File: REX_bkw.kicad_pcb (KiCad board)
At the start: 2 copper layers, 16 x 38 mm, 11 parts, among them J1 Molex_DIP28_edge_contacts, J2 JTAG, J3 PRG, U1 XCR3064XL-10VQ44, U2 29F800, U3 LP2980

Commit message: names
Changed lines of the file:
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@@
   (layers
     (0 Top signal)
-    (31 Bottom signal hide)
+    (31 Bottom signal)
     (32 B.Adhes user hide)
     (33 F.Adhes user hide)
@@
     (descr "Castellated edge contacts to fit Molex 8878 Socket")
     (solder_mask_margin -0.28)
+    (attr virtual)
     (fp_text reference J1 (at -0.9906 -0.9906 -90) (layer Dwgs.User) hide
       (effects (font (size 1.2065 1.2065) (thickness 0.127)) (justify left bottom))
@@
     (descr "Castellated edge contacts to fit Molex 8878 Socket")
     (solder_mask_margin -0.28)
+    (attr virtual)
     (fp_text reference carrier? (at -1.5 0 -90) (layer Dwgs.User) hide
       (effects (font (size 1.2065 1.2065) (thickness 0.127)) (justify left bottom))
@@
     (descr "jamb connector, 4 pin, staggered")
     (solder_mask_margin -0.17272)
-    (fp_text reference J3 (at -1.332036 -1.850661 -180) (layer Dwgs.User)
-      (effects (font (size 1.2065 1.2065) (thickness 0.127)) (justify right bottom))
+    (fp_text reference J3 (at 0 0 -180) (layer Dwgs.User)
+      (effects (font (size 1.2065 1.2065) (thickness 0.127)) (justify bottom))
     )
     (fp_text value PRG (at 0.039564 2.518139 unlocked) (layer F.Fab)
@@
     (descr "6 pin jamb connector, perpendicular offsets")
     (solder_mask_margin -0.17272)
-    (fp_text reference J2 (at -1.288539 -1.699304 -180) (layer Dwgs.User)
-      (effects (font (size 1.2065 1.2065) (thickness 0.127)) (justify right bottom))
+    (fp_text reference J2 (at 0 0 -180) (layer Dwgs.User)
+      (effects (font (size 1.2065 1.2065) (thickness 0.127)) (justify bottom))
     )
     (fp_text value JTAG (at 0.057661 2.669496 unlocked) (layer F.Fab)
@@
     (tags "TSOP I 32")
     (attr smd)
-    (fp_text reference U2 (at -1.58496 -0.44958 90) (layer B.SilkS)
+    (fp_text reference U2 (at -1.58496 -0.44958 90) (layer B.SilkS) hide
       (effects (font (size 1.2065 1.2065) (thickness 0.1016)) (justify left bottom mirror))
     )
@@
     (at 147.1168 99.187 270)
     (attr smd)
-    (fp_text reference U1 (at -1.4859 0.2667 270 unlocked) (layer F.SilkS)
+    (fp_text reference U1 (at -1.4859 0.2667 270 unlocked) (layer F.SilkS) hide
       (effects (font (size 1.2065 1.2065) (thickness 0.1016)) (justify left bottom))
     )

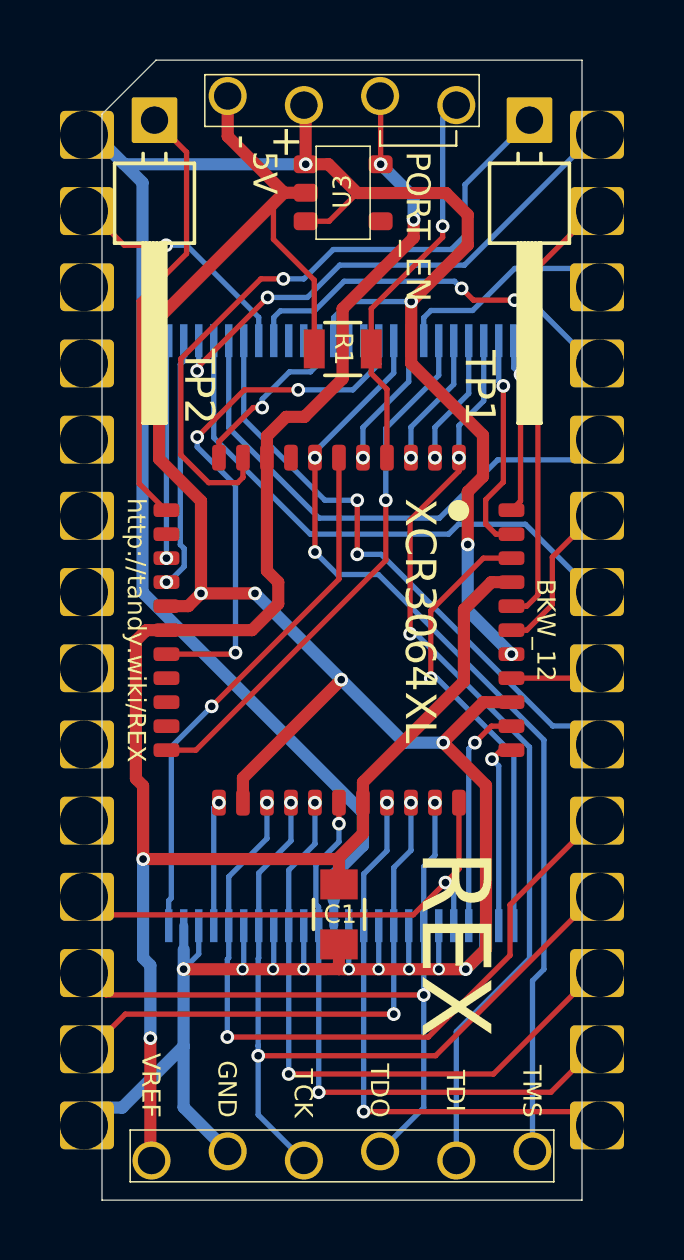
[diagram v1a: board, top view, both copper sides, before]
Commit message: remove some sharp inside angles. move c1 on nec.
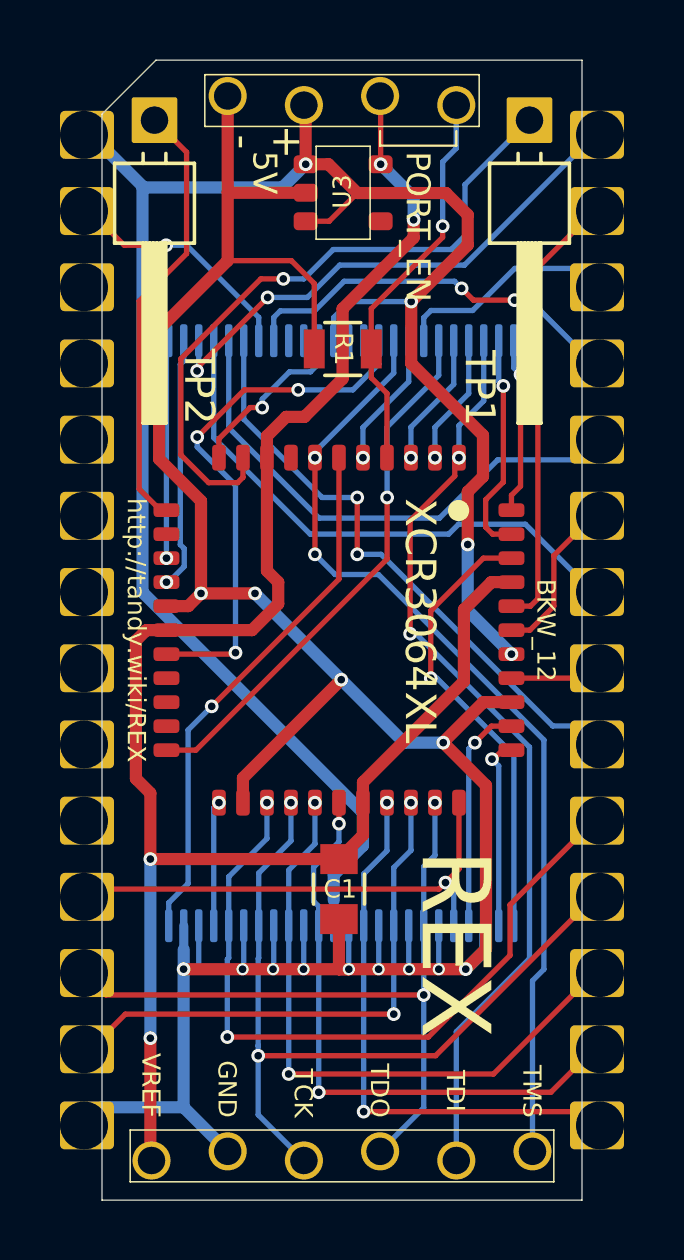
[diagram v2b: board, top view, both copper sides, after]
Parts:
- moved C1 0.84 mm to (147.1, 107.8)
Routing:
- net /+5: track 69.6 -> 67.8 mm
- net +3V3: track 62.1 -> 61.0 mm
- net GND: track 90.3 -> 91.2 mm
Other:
- board text added: "R1: 10k - 47k"
- board text removed: "R1: 10k"

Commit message: v13
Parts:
- added NT1: Net-Tie_2, 000_LOCAL:Net_Tie_2_0.18mm, F.Cu at (146.8, 85.7)
- added NT2: Net-Tie_2, 000_LOCAL:Net_Tie_2_0.18mm, B.Cu at (142.0, 109.8)
- added NT3: Net-Tie_2, 000_LOCAL:Net_Tie_2_0.18mm, B.Cu at (144.5, 114.6)
- added NT4: Net-Tie_2, 000_LOCAL:Net_Tie_2_0.18mm, B.Cu at (150.0, 114.6)
- added NT5: Net-Tie_2, 000_LOCAL:Net_Tie_2_0.18mm, B.Cu at (151.0, 115.7)
- added NT6: Net-Tie_2, 000_LOCAL:Net_Tie_2_0.18mm, B.Cu at (153.6, 114.6)
- C1: footprint Capacitors_SMD:C_0805 -> 000_LOCAL:C_0805
- R1: footprint Resistors_SMD:R_0805 -> 000_LOCAL:R_0805
- moved U2 0.10 mm to (147.2, 99.2)
- moved U1 0.10 mm to (147.2, 99.2)
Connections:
- net /AD0 renamed /D0
- net /AD2 renamed /D2
- net /AD3 renamed /D3
- net /AD4 renamed /D4
- net /AD5 renamed /D5
- net /AD7 renamed /D7
- J1 pad 12: /AD1 -> /D1
- J1 pad 18: /AD6 -> /D6
- J2 pad 3: /AD6 -> /TCK
- J2 pad 4: /AD1 -> /TDO
- J2 pad 5: /LVA4 -> /TDI
- J2 pad 6: /LVA19 -> /TMS
- U1 pad 26: /AD6 -> /D6
- U1 pad 32: /AD1 -> /D1
- U1 pad 38: /+5 -> /~RESET
- U2 pad 12: /+5 -> /~RESET
- U2 pad 31: /AD1 -> /D1
- U2 pad 42: /AD6 -> /D6
- U2 pad 47: GND -> /~BYTE
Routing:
- net /+5: track 67.8 -> 41.0 mm, vias 4 -> 1
- net /AD6: track 26.6 -> 0.00 mm, vias 2 -> 0
- net /AD1: track 24.0 -> 0.00 mm, vias 2 -> 0
- net /D6: track 0.00 -> 23.0 mm, vias 0 -> 2
- net /D1: track 0.00 -> 21.2 mm, vias 0 -> 2
- net /~RESET: track 0.00 -> 19.7 mm, vias 0 -> 4
- net GND: track 91.2 -> 85.2 mm, vias 13 -> 12
- net /TP1: track 22.3 -> 17.4 mm
- net /TCK: track 0.00 -> 2.79 mm
- net /D7: track 24.8 -> 22.0 mm
- net /RY_BY: track 17.5 -> 14.8 mm, vias 3 -> 1
- net /TDO: track 0.00 -> 2.49 mm
- net +3V3: track 61.0 -> 58.8 mm, vias 4 -> 2
- net /D5: track 21.2 -> 19.0 mm
- net /LVA19: track 32.3 -> 30.3 mm
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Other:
- net class Default: clearance 0.1778 -> 0.16; trace_width 0.1778 -> 0.18; via_dia 0.4572 -> 0.4; via_drill 0.254 -> 0.25
- rule trace_clearance: 0.1778 -> 0.16
- rule trace_min: 0.1778 -> 0.16
- rule via_min_drill: 0.254 -> 0.25
- rule via_min_size: 0.381 -> 0.4
- board text added: "BKW_13"
- board text removed: "BKW_12"

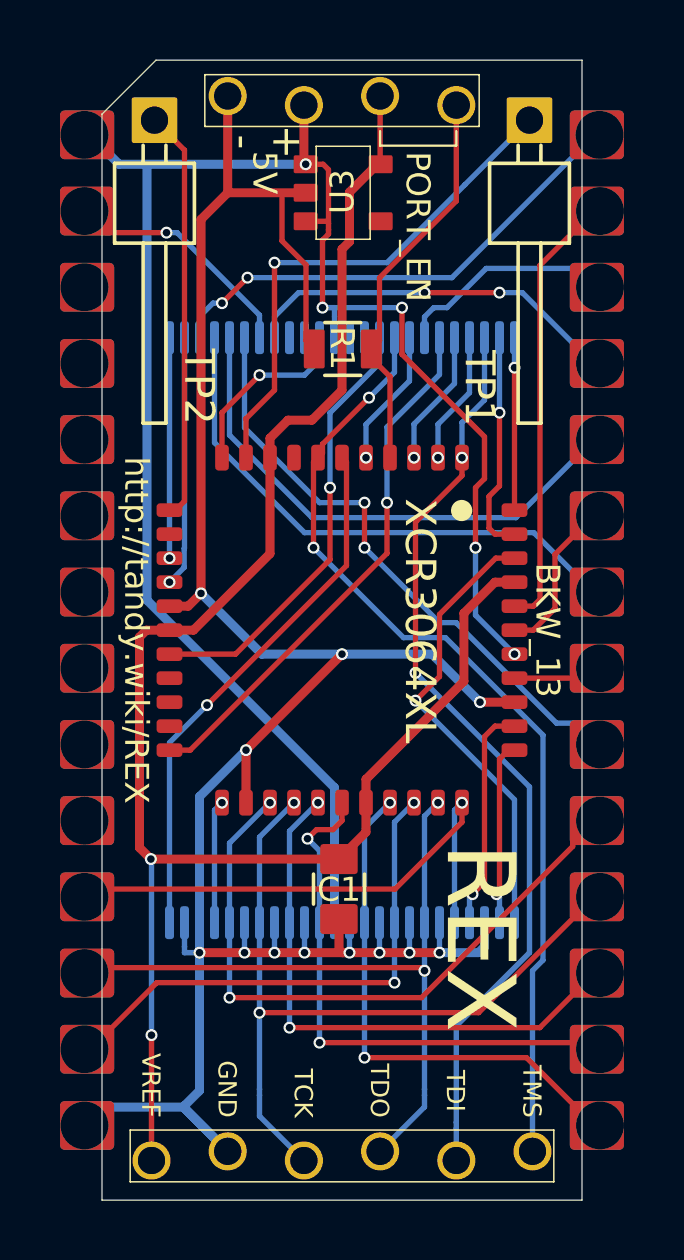
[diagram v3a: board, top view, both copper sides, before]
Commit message: flip ram and reroute nec board, several other minor touches both boards
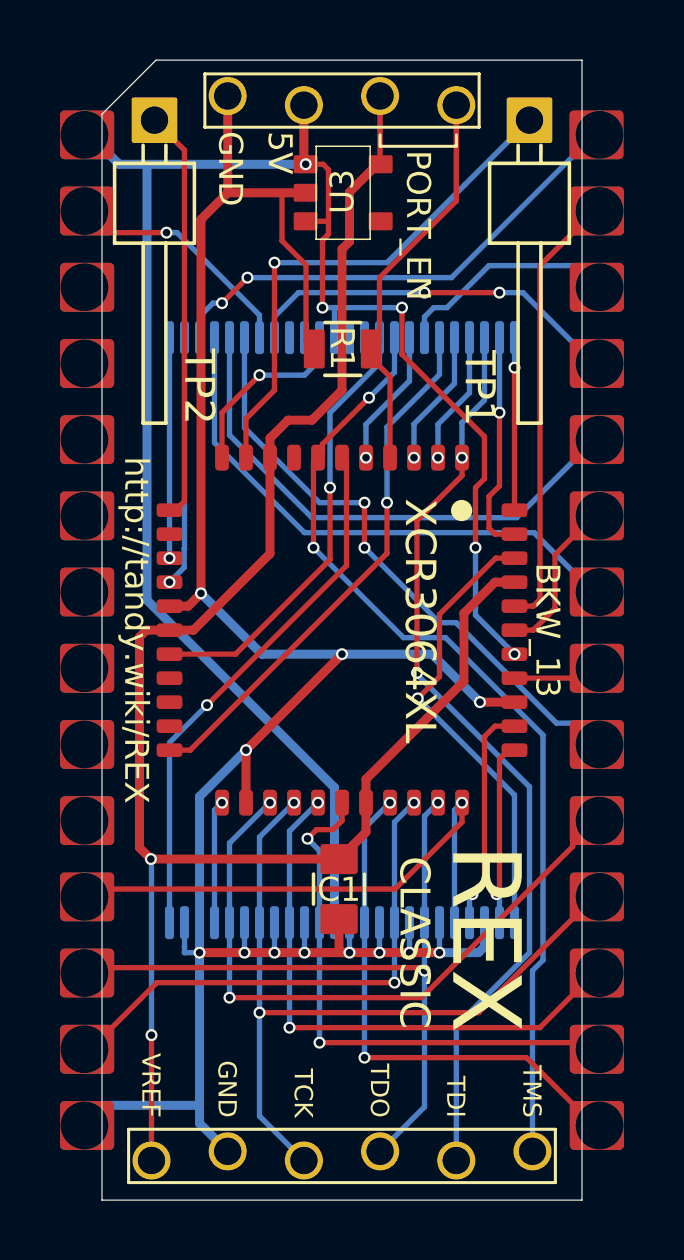
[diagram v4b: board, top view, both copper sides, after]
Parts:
- removed NT3, NT4, NT5, NT6: Net-Tie_2, 000_LOCAL:Net_Tie_2_0.18mm
- R1: value 10k -> 47k
- U3: value LP2980 -> LP2980-3.3
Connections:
- J2 pad 3: /TCK -> /D6
- J2 pad 4: /TDO -> /D1
- J2 pad 5: /TDI -> /LVA4
- J2 pad 6: /TMS -> /LVA19
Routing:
- net /D6: track 23.0 -> 26.0 mm
- net /TCK: track 2.79 -> 0.00 mm
- net /D1: track 21.2 -> 23.9 mm
- net /TDO: track 2.49 -> 0.00 mm
- net /LVA19: track 30.3 -> 32.4 mm
- net /TMS: track 1.87 -> 0.00 mm
- net GND: track 85.2 -> 83.9 mm
- net /LVA4: track 29.7 -> 30.9 mm
- net /TDI: track 1.07 -> 0.00 mm
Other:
- board text added: "CLASSIC"
- board text added: "R1: 47k"
- board text removed: "+"
- board text removed: "-"
- board text removed: "R1: 10k - 47k"
